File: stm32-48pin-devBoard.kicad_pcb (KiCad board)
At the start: 2 copper layers, 83.8 x 48.3 mm, 44 parts, among them J1 USB, M1 Mounting Hole, M2 Mounting Hole, M3 Mounting Hole, M4 Mounting Hole, P1 USB-DISCONNECT, P2 VBAT, P3 VSEL, P4 BOOT0, P5 JTAG10, P6 P24, P7 P24, U1 ZXMP2120FFTA, U2 ZLDO1117, U3 STM32-48PIN, X1 32kHz, X2 8MHz

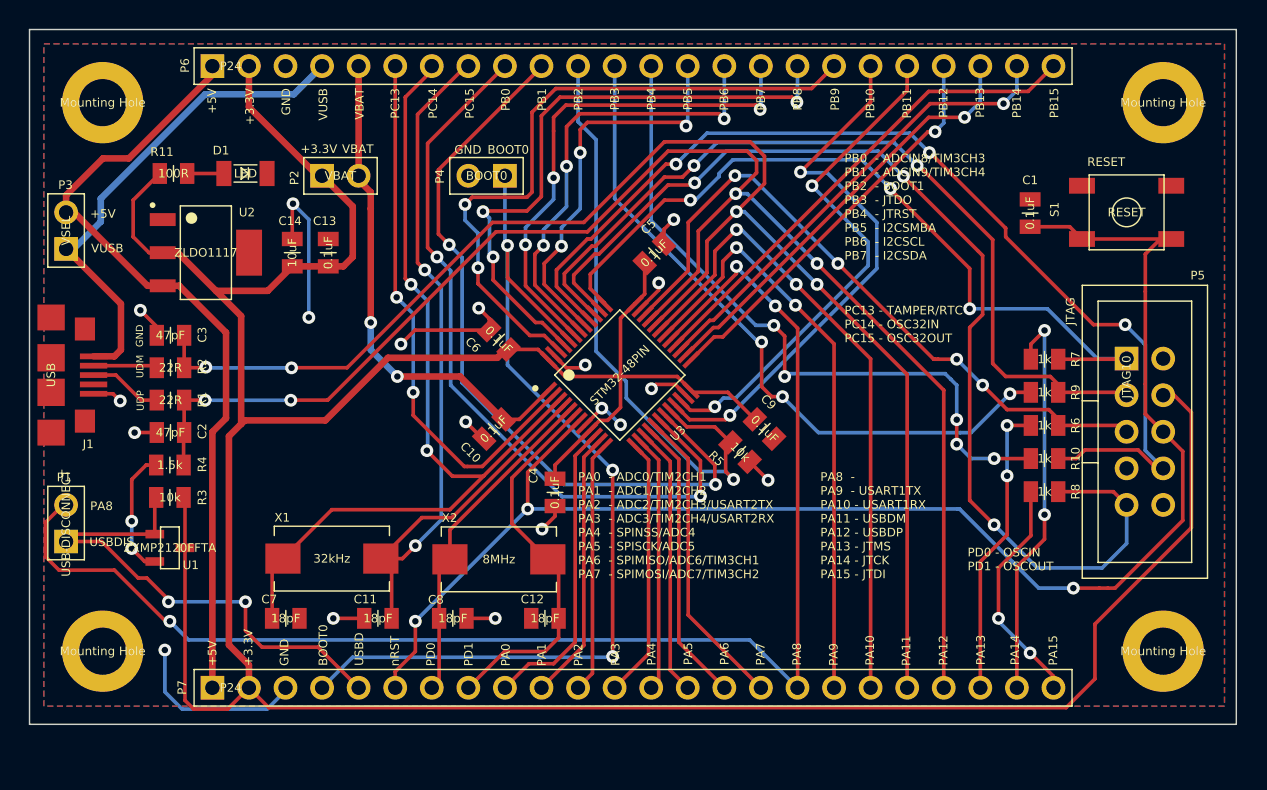
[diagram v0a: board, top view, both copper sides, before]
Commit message: switch to new kicad mod format and started rework
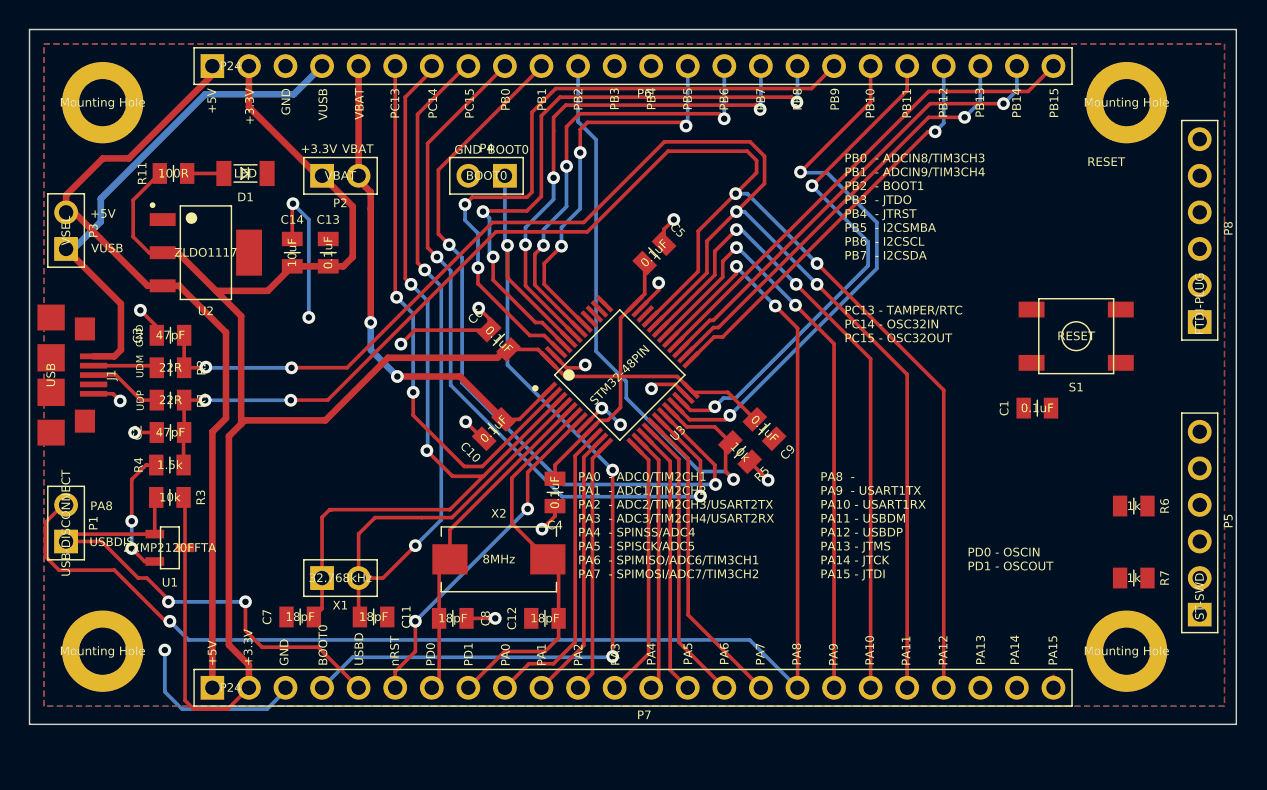
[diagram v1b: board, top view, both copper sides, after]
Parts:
- removed R10, R8, R9: 1k, stm32:RESC2012X100N
- added P8: FTDI-PLUG, kicadlib:HDRV6W66P254_1X6_1524X249X838P, F.Cu at (205.7, 68.6)
- C1, C10, C11, C12, C13, C14, C2, C3, C4, C5, C6, C7, C8, C9: footprint stm32:CAPC2012X100N -> kicadlib:CAPC2012X100N
- D1: footprint stm32:LEDC3216X100N -> kicadlib:LEDC3216X100N
- J1: footprint stm32:JST_UB-MC5BR3-SD204-4S-NMP -> kicadlib:JST_UB-MC5BR3-SD204-4S-NMP
- M1, M2, M3, M4: footprint stm32:MTGNP565H328Z565P -> kicadlib:MTGNP565H328Z565P
- P1, P2, P3, P4: footprint stm32:HDRV2W66P254_1X2_508X249X838P -> kicadlib:HDRV2W66P254_1X2_508X249X838P
- P5: value JTAG10 -> ST-SWD; footprint stm32:SHDRV10W66P254_2X5_2035X870X609P -> kicadlib:HDRV6W66P254_1X6_1524X249X838P
- P6, P7: footprint stm32:HDRV24W66P254_1X24_6096X249X838P -> kicadlib:HDRV24W66P254_1X24_6096X249X838P
- R1, R11, R2, R3, R4, R5, R6, R7: footprint stm32:RESC2012X100N -> kicadlib:RESC2012X100N
- S1: footprint stm32:CKCOMP-PTS525SM10SMTR -> kicadlib:CKCOMP-PTS525SM10SMTR
- U1: footprint stm32:SOT95P237X112_123-3N -> kicadlib:SOT95P237X112_123-3N
- U2: footprint stm32:SOT230P700X180-4N -> kicadlib:SOT230P700X180-4N
- U3: footprint stm32:QFP50P900X900X160-48N -> kicadlib:QFP50P900X900X160-48N
- X1: value 32kHz -> 32.768kHz; footprint stm32:XTAL8045X200N -> kicadlib:HDRV2W66P254_1X2_508X249X838P
- X2: footprint stm32:XTAL8045X200N -> kicadlib:XTAL8045X200N
- moved P5 18.5 mm to (205.7, 88.9), turned to 90 degrees
- moved R7 16.4 mm to (201.2, 86.4)
- moved C1 13.6 mm to (194.5, 74.6), turned to 180 degrees
- moved S1 9.28 mm to (197.2, 69.6)
- moved R6 8.35 mm to (201.2, 81.4)
- moved M1 2.54 mm to (200.7, 53.3)
- moved M2 2.54 mm to (200.7, 91.4)
- moved X1 1.51 mm to (144.8, 86.4), turned to 0 degrees
- moved C7 1.00 mm to (143.3, 89.1), turned to 180 degrees
- moved C11 0.32 mm to (148.4, 89.1), turned to 0 degrees
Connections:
- P5 pad 1: /JTCK -> +3.3V
- P5 pad 2: GND -> /SWCLK
- P5 pad 3: /JTDO -> GND
- P5 pad 4: +3.3V -> /SWDIO
- P5 pad 5: /JTMS -> /nRST
- P5 pad 6: /nRST -> Net-(P5-Pad6)
- R6 pad 2: /JTMS -> /SWDIO
- R7 pad 2: /JTCK -> /SWCLK
- U3 pad 34: /JTMS -> /SWDIO
- U3 pad 37: /JTCK -> /SWCLK
- U3 pad 38: /JTDI -> /PA15
- U3 pad 39: /JTDO -> /PB3
- U3 pad 40: /JNTRST -> /PB4
- X1 pad 1: /PC15 -> /PC14
- X1 pad 2: /PC14 -> /PC15
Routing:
- net +3.3V: track 229.7 -> 145.8 mm
- net /nRST: track 105.5 -> 23.8 mm, vias 3 -> 2
- net /JTDI: track 76.8 -> 0.00 mm, vias 3 -> 0
- net /JNTRST: track 72.8 -> 0.00 mm, vias 3 -> 0
- net /JTDO: track 59.1 -> 0.00 mm, vias 2 -> 0
- net /JTCK: track 55.3 -> 0.00 mm, vias 3 -> 0
- net /PB4: track 48.2 -> 0.02 mm, vias 5 -> 0
- net /PB3: track 47.8 -> 0.02 mm, vias 3 -> 0
- net /JTMS: track 47.0 -> 0.00 mm, vias 4 -> 0
- net /PA14: track 28.0 -> 0.00 mm, vias 2 -> 0
- net /PA13: track 20.6 -> 0.00 mm, vias 2 -> 0
- net /PA15: track 16.1 -> 0.82 mm, vias 2 -> 0
- net /PC15: track 60.7 -> 64.9 mm
- net GND: track 60.5 -> 58.4 mm, vias 19 -> 18
- net /PC14: track 61.0 -> 59.8 mm
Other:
- board text removed: "JTAG"

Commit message: re-route based on new issues
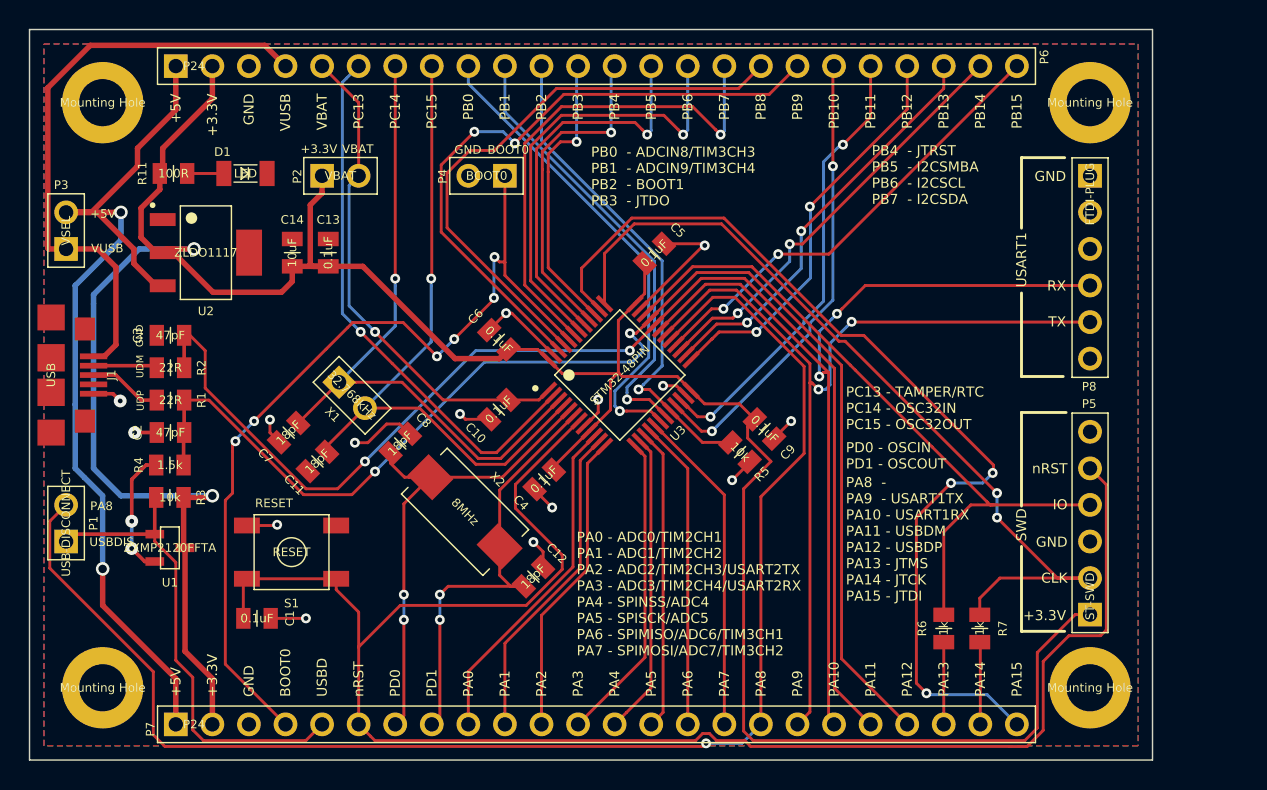
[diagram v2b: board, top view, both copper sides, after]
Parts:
- moved S1 56.5 mm to (142.7, 84.6)
- moved C1 56.1 mm to (140.3, 89.2), turned to 0 degrees
- moved R6 15.7 mm to (188.0, 89.9), turned to 90 degrees
- moved X1 13.7 mm to (146.0, 72.8), turned to 315 degrees
- moved C7 12.8 mm to (142.5, 76.3), turned to 225 degrees
- moved P8 12.7 mm to (198.1, 58.4), turned to 270 degrees
- moved C8 12.7 mm to (150.2, 77.0), turned to 45 degrees
- moved C11 11.5 mm to (144.5, 78.3), turned to 225 degrees
- moved R7 11.3 mm to (190.5, 89.9), turned to 90 degrees
- moved P5 7.62 mm to (198.1, 88.9)
- moved X2 4.05 mm to (154.7, 81.8), turned to 135 degrees
- moved M2 3.59 mm to (198.1, 94.0)
- moved P7 3.59 mm to (134.6, 96.5)
- moved C12 3.01 mm to (159.5, 86.3), turned to 45 degrees
- moved M3 2.54 mm to (129.5, 94.0)
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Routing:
- net /nRST: track 23.8 -> 120.5 mm, vias 2 -> 0
- net /PA15: track 0.82 -> 67.3 mm, vias 0 -> 3
- net /SWCLK: track 0.06 -> 58.7 mm, vias 0 -> 2
- net +3.3V: track 145.8 -> 195.5 mm, vias 0 -> 2
- net /SWDIO: track 0.03 -> 49.1 mm
- net /PB4: track 0.02 -> 23.0 mm, vias 0 -> 1
- net /PB1: track 52.4 -> 31.4 mm, vias 2 -> 1
- net /PA9: track 41.5 -> 62.1 mm
- net /PB3: track 0.02 -> 20.1 mm, vias 0 -> 1
- net /PA10: track 45.0 -> 64.1 mm
- net /PB0: track 52.0 -> 33.5 mm, vias 2 -> 1
- net /PC15: track 64.9 -> 47.3 mm, vias 2 -> 1
- net /PA12: track 106.6 -> 90.8 mm, vias 4 -> 2
- net /PA11: track 102.6 -> 87.8 mm, vias 4 -> 2
- net GND: track 58.4 -> 44.4 mm, vias 18 -> 15
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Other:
- board size 83.8 x 48.3 mm -> 78 x 50.7 mm
- net class Default: trace_width 0.254 -> 0.2032; via_dia 0.889 -> 0.6858; via_drill 0.635 -> 0.3302
- net class power added: clearance 0.254, trace_width 0.381, via_dia 0.9398, via_drill 0.5842
- rule trace_min: 0.254 -> 0.1524
- rule via_min_drill: 0.508 -> 0.3302
- rule via_min_size: 0.889 -> 0.6858
- board text added: "2014-08-17"
- board text added: "CLK"
- board text added: "IO"
- board text added: "PB0 - ADCIN8/TIM3CH3 PB1 - ADCIN9/TIM3CH4 PB2 - BOOT1 PB3 - JTDO"
- board text added: "PB4 - JTRST PB5 - I2CSMBA PB6 - I2CSCL PB7 - I2CSDA"
- board text added: "RX"
- board text added: "SWD"
- board text added: "TX"
- board text added: "USART1"
- board text removed: "2013-10-24"
- board text removed: "PB0 - ADCIN8/TIM3CH3 PB1 - ADCIN9/TIM3CH4 PB2 - BOOT1 PB3 - JTDO PB4 - JTRST PB5 - I2CSMBA PB6 - I2CSCL PB7 - I2CSDA"
